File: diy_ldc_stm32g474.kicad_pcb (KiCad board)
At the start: 2 copper layers, 50.2 x 40 mm, 91 parts, among them J1 USB_B_Micro, J10 Conn_02x03_Odd_Even, J12 Conn_01x04, J13 Conn_01x05, J2 Conn_01x02, J3 Conn_01x03, J4 Conn_01x04, J6 Conn_Coaxial, J7 Conn_Coaxial, J8 Conn_Coaxial, J9 Conn_Coaxial, U1 XC6206PxxxMR, U2 STM32G431CBUx, U3 SN74LVC2G14DBV, U4 SN74LVC2G14DBV, U5 TPH2502-SR, U6 TLV2333IDR, U7 TPS61040DBV, U8 OPA2188AIDR, Y1 24MHz, 9pF

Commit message: WIP
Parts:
- moved C23 0.80 mm to (171.9, 71.5)
- moved R11 0.80 mm to (176.0, 73.9)
- moved R12 0.80 mm to (172.7, 73.9)
- moved R13 0.80 mm to (174.4, 73.9)
- moved R14 0.80 mm to (171.1, 73.9)
- moved H1 0.07 mm to (143.2, 63.4)
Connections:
- L1 pad 2: +3.3V -> +3V3
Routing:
- net GND: track 0.00 -> 10.1 mm, vias 0 -> 15
- net Net-(U2-PF0): track 0.00 -> 6.36 mm
- net +5V_IN: track 0.00 -> 5.69 mm
- net +3V3: track 0.00 -> 5.38 mm, vias 0 -> 4
- net Net-(C13-Pad1): track 0.00 -> 4.92 mm
- net /MCU/VREF+: track 0.00 -> 4.02 mm
- net Net-(U8B--): track 0.00 -> 3.69 mm
- net Net-(U8A--): track 0.00 -> 3.68 mm
- net +18V: track 0.00 -> 2.83 mm
- net +5V: track 0.00 -> 2.74 mm
- net Net-(U2-PF1): track 0.00 -> 2.24 mm
- net /MCU/piezo_drive/DAC1_CH1_GAIN: track 0.00 -> 2.22 mm
- net /MCU/NRST: track 0.00 -> 1.30 mm
- net /MCU/BOOT0: track 0.00 -> 1.26 mm
- added copper zone on F.Cu, net +3V3
- added copper zone on In2.Cu, net +3V3
- added copper zone on F.Cu, net +5V
- added copper zone on F.Cu, net +5V_IN
- added copper zone on F.Cu, net GND
- added copper zone on In1.Cu, net GND
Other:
- copper layers 2 -> 4
- board text added: "CLK"
- board text added: "DIO"
- board text added: "INV OUT0"
- board text added: "INV OUT1"
- board text removed: "INV_OUT0"
- board text removed: "INV_OUT1"

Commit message: Routing
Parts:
- moved J12 7.78 mm to (188.4, 78.8), turned to 180 degrees
- moved C31 3.88 mm to (153.3, 90.3), turned to -90 degrees
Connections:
- net Net-(U2-PA11) renamed /MCU/USB_MCU_D-
- net Net-(U2-PA12) renamed /MCU/USB_MCU_D+
- J1 pad 2: /MCU/Power/USB_D- -> /MCU/USB_D-
- J1 pad 3: /MCU/Power/USB_D+ -> /MCU/USB_D+
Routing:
- net +5V: track 2.74 -> 41.1 mm, vias 0 -> 4
- net +18V: track 2.83 -> 18.6 mm
- net /MCU/piezo_record_needle/PIEZO_IN_B: track 0.00 -> 15.0 mm
- net /MCU/piezo_drive/DAC1_CH1_GAIN: track 2.22 -> 17.1 mm
- net /MCU/USB_D-: track 0.00 -> 11.6 mm
- net /MCU/USB_D+: track 0.00 -> 11.1 mm
- net /MCU/piezo_record_needle/Vhalf: track 0.00 -> 10.8 mm
- net /MCU/piezo_drive/DAC1_CH2_GAIN: track 0.00 -> 8.81 mm
- net Net-(U5A--): track 0.00 -> 7.73 mm
- net +3V3: track 5.38 -> 11.6 mm, vias 4 -> 8
- net /MCU/piezo_record_needle/PIEZO_IN_A: track 0.00 -> 6.03 mm
- net GND: track 10.1 -> 4.32 mm, vias 15 -> 2
- net Net-(U6B--): track 0.00 -> 5.60 mm
- net Net-(U6A--): track 0.00 -> 5.43 mm
- net Net-(U7-FB): track 0.00 -> 5.07 mm
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- added copper zone on F.Cu, net +18V
- added copper zone on F.Cu, net Net-(D3-A)

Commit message: Preliminary routing done
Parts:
- moved J9 12.9 mm to (161.3, 64.0)
- moved J8 12.8 mm to (174.0, 64.0)
- moved C22 7.66 mm to (164.5, 77.2)
- moved R17 4.07 mm to (158.8, 73.5), turned to 90 degrees
- moved R18 1.85 mm to (162.0, 73.5)
- moved R16 1.47 mm to (160.4, 73.5)
- moved R15 1.31 mm to (157.3, 73.5)
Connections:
- J10 pad 1: /MCU/SPI3_SCK -> /MCU/SPI3_MISO
- J10 pad 3: /MCU/SPI3_MOSI -> /MCU/SPI3_SCK
- J10 pad 5: /MCU/SPI3_MISO -> /MCU/SPI3_MOSI
- J13 pad 1: /MCU/piezo_drive/dac1_out1 -> /MCU/dac1_out2
- J13 pad 2: /MCU/piezo_drive/dac1_out2 -> /MCU/dac1_out1
- J4 pad 2: /MCU/opamp2_vinp -> /MCU/opamp3_vinp
- J4 pad 3: /MCU/opamp3_vinp -> /MCU/opamp2_vinp
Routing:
- net /MCU/TIM4_ETR: track 0.00 -> 38.7 mm, vias 0 -> 2
- net GND: track 4.32 -> 42.5 mm, vias 2 -> 43
- net /MCU/opamp1_vinp: track 3.77 -> 40.1 mm, vias 0 -> 3
- net /MCU/TIM3_ETR: track 0.00 -> 34.5 mm
- net /MCU/SPI3_MISO: track 0.00 -> 34.4 mm, vias 0 -> 1
- net /MCU/SPI3_SCK: track 0.00 -> 33.1 mm, vias 0 -> 1
- net /MCU/opamp2_vinp: track 3.85 -> 36.7 mm, vias 0 -> 2
- net /MCU/BOOST_EN: track 0.00 -> 31.2 mm
- net /MCU/SPI3_MOSI: track 0.00 -> 29.4 mm, vias 0 -> 1
- net /MCU/TIM1_ETR: track 4.31 -> 32.4 mm, vias 0 -> 4
- net /MCU/dac1_out2: track 0.00 -> 20.9 mm, vias 0 -> 2
- net /MCU/dac1_out1: track 0.00 -> 20.2 mm, vias 0 -> 2
- net /MCU/TIM2_ETR: track 0.00 -> 17.2 mm
- net Net-(J7-In): track 0.00 -> 13.9 mm
- net /MCU/opamp3_vinp: track 0.00 -> 13.7 mm
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
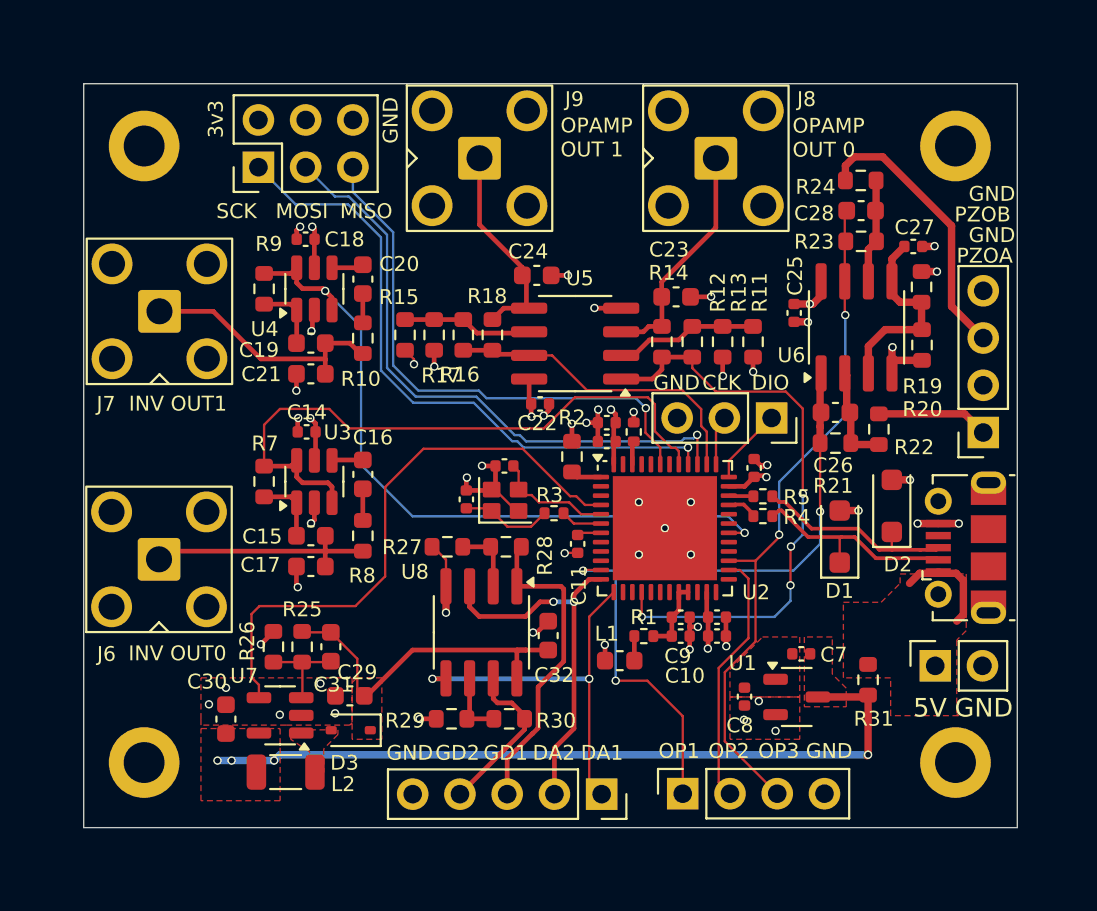
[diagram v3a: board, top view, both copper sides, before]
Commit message: changed 1 instance of Inverter oscillator
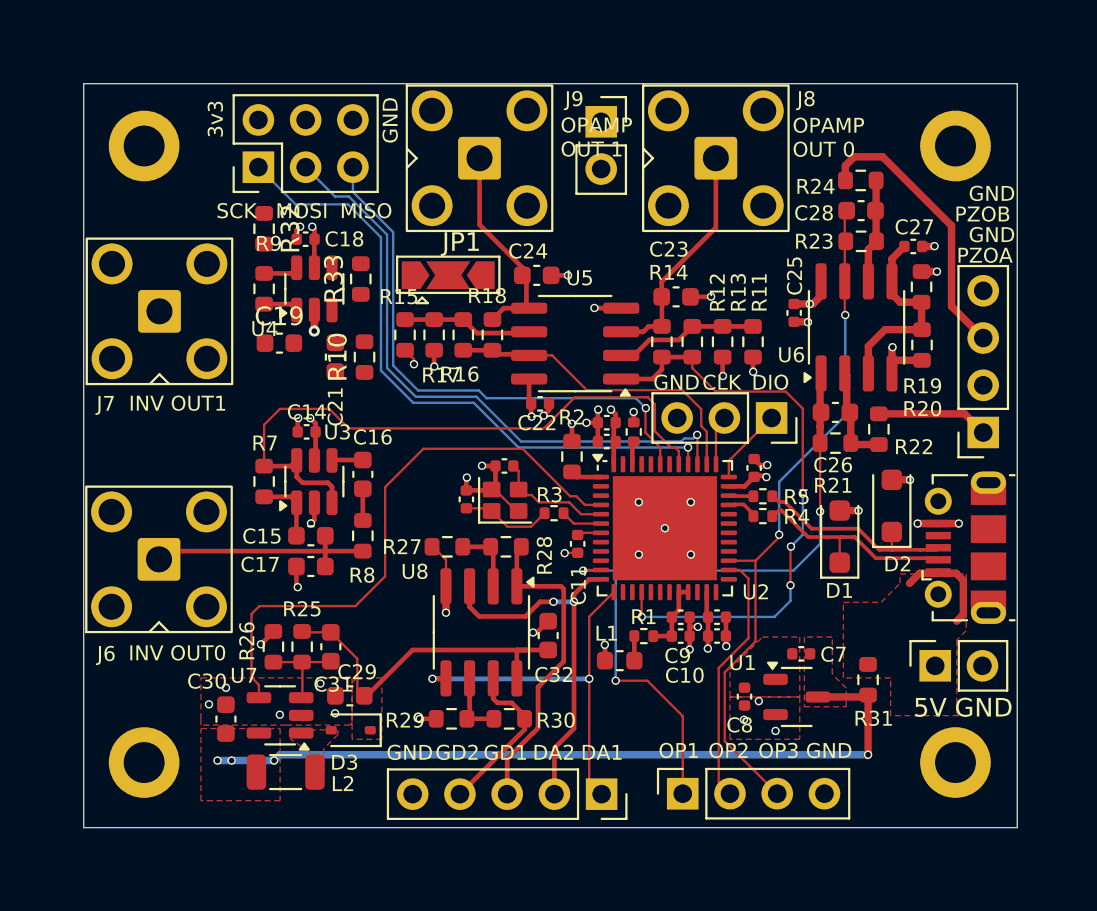
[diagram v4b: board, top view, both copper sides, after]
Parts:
- removed C20: 10n, Capacitor_SMD:C_0603_1608Metric
- added J5: Conn_01x02, Connector_PinSocket_2.54mm:PinSocket_1x02_P2.54mm_Vertical, F.Cu at (167.8, 62.0)
- added JP1: SolderJumper_3_Open, Jumper:SolderJumper-3_P2.0mm_Open_TrianglePad1.0x1.5mm, F.Cu at (159.6, 70.3)
- added R32: 49.9, Resistor_SMD:R_0603_1608Metric, F.Cu at (149.7, 67.8)
- added R33: 49.9, Resistor_SMD:R_0603_1608Metric, F.Cu at (154.9, 70.5)
- C19: value 10n -> 1n
- R10: value 10k -> 10Meg
- moved C19 1.69 mm to (150.5, 74.0), turned to 0 degrees
- moved C21 1.60 mm to (153.5, 74.7), turned to 90 degrees
- moved R10 1.02 mm to (155.1, 74.7), turned to 90 degrees
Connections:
- C21 pad 1: GND -> Net-(J5-Pin_2)
- C21 pad 2: Net-(J7-In) -> Net-(U4-2A)
- J7 pad 2: GND -> Net-(J7-Ext)
- R10 pad 1: Net-(C20-Pad2) -> GND
- R10 pad 2: Net-(J7-In) -> Net-(U4-2A)
- R9 pad 1: Net-(U4-1A) -> GND
- R9 pad 2: /MCU/TIM4_ETR -> Net-(U4-1A)
- U4 pad 3: /MCU/TIM4_ETR -> Net-(U4-2A)
- U4 pad 4: Net-(U4-2Y) -> /MCU/logic_gate_ldc/out2
- U4 pad 6: /MCU/TIM4_ETR -> /MCU/logic_gate_ldc/out1
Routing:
- net /MCU/TIM4_ETR: track 38.7 -> 1.88 mm, vias 2 -> 0
- net Net-(J7-In): track 13.9 -> 0.00 mm
- net Net-(U4-1A): track 3.67 -> 1.88 mm
- net Net-(U4-2Y): track 1.72 -> 0.00 mm
- net Net-(C20-Pad2): track 1.58 -> 0.00 mm
- net GND: track 42.5 -> 41.6 mm, vias 43 -> 42

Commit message: routing
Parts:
- moved C19 5.61 mm to (149.7, 68.4), turned to 90 degrees
- moved R32 1.62 mm to (151.2, 68.4)
- moved C18 1.45 mm to (152.9, 69.4), turned to 0 degrees
- moved R33 1.43 mm to (154.9, 71.9)
- moved R9 1.03 mm to (149.7, 72.1)
- moved U4 1.03 mm to (152.4, 72.1)
- moved C21 1.03 mm to (153.5, 75.7)
- moved R10 1.03 mm to (155.1, 75.7)
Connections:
- C19 pad 1: Net-(J7-In) -> Net-(J7-Ext)
- C19 pad 2: Net-(U4-1A) -> Net-(C19-Pad2)
- R32 pad 1: Net-(J7-Ext) -> Net-(C19-Pad2)
- R9 pad 2: Net-(U4-1A) -> Net-(J7-In)
- U4 pad 1: Net-(U4-1A) -> Net-(J7-In)
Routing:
- net Net-(J7-Ext): track 0.00 -> 18.6 mm
- net Net-(J7-In): track 0.00 -> 9.05 mm
- net Net-(U4-1A): track 1.88 -> 0.00 mm
- net /MCU/TIM4_ETR: track 1.88 -> 0.00 mm
- net /MCU/logic_gate_ldc/out1: track 0.00 -> 1.80 mm
- net /MCU/logic_gate_ldc/out2: track 0.00 -> 1.62 mm
- net Net-(C19-Pad2): track 0.00 -> 1.52 mm

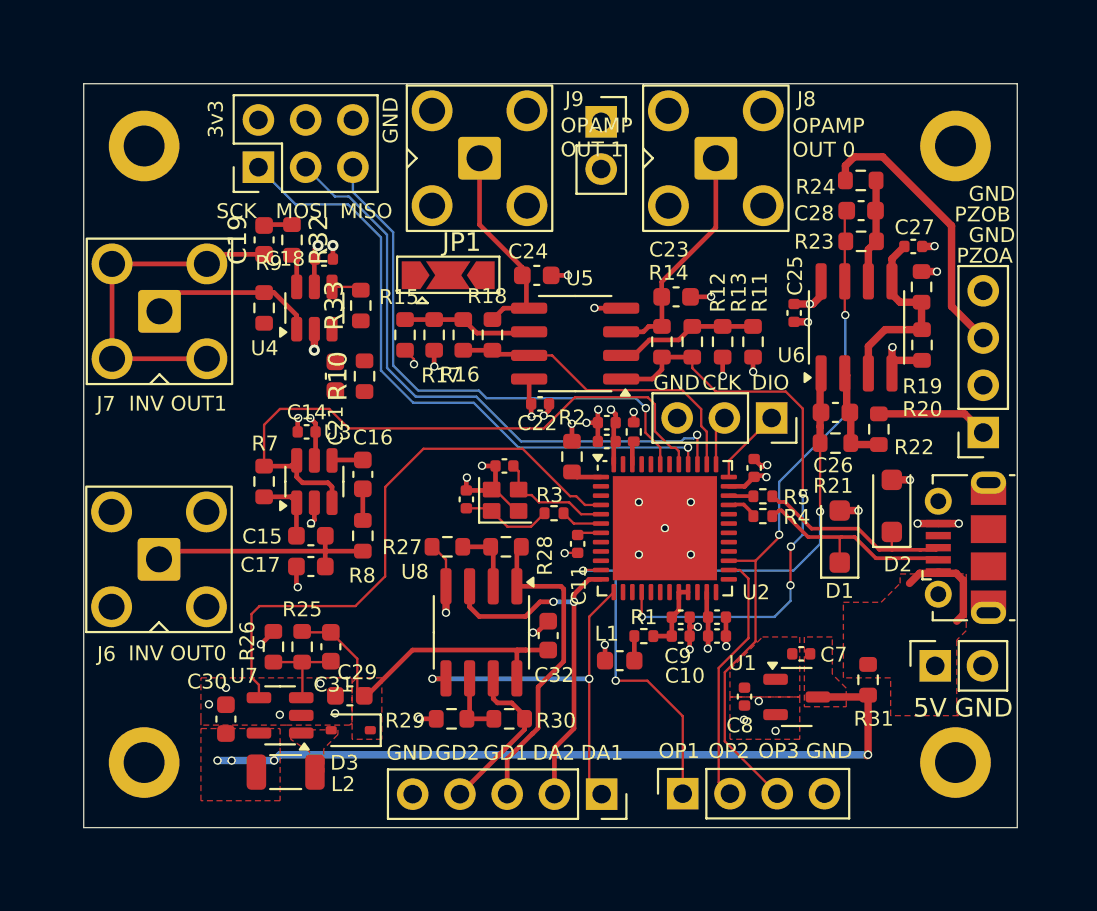
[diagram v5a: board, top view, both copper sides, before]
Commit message: Finisher re-routing with new inverter oscillators
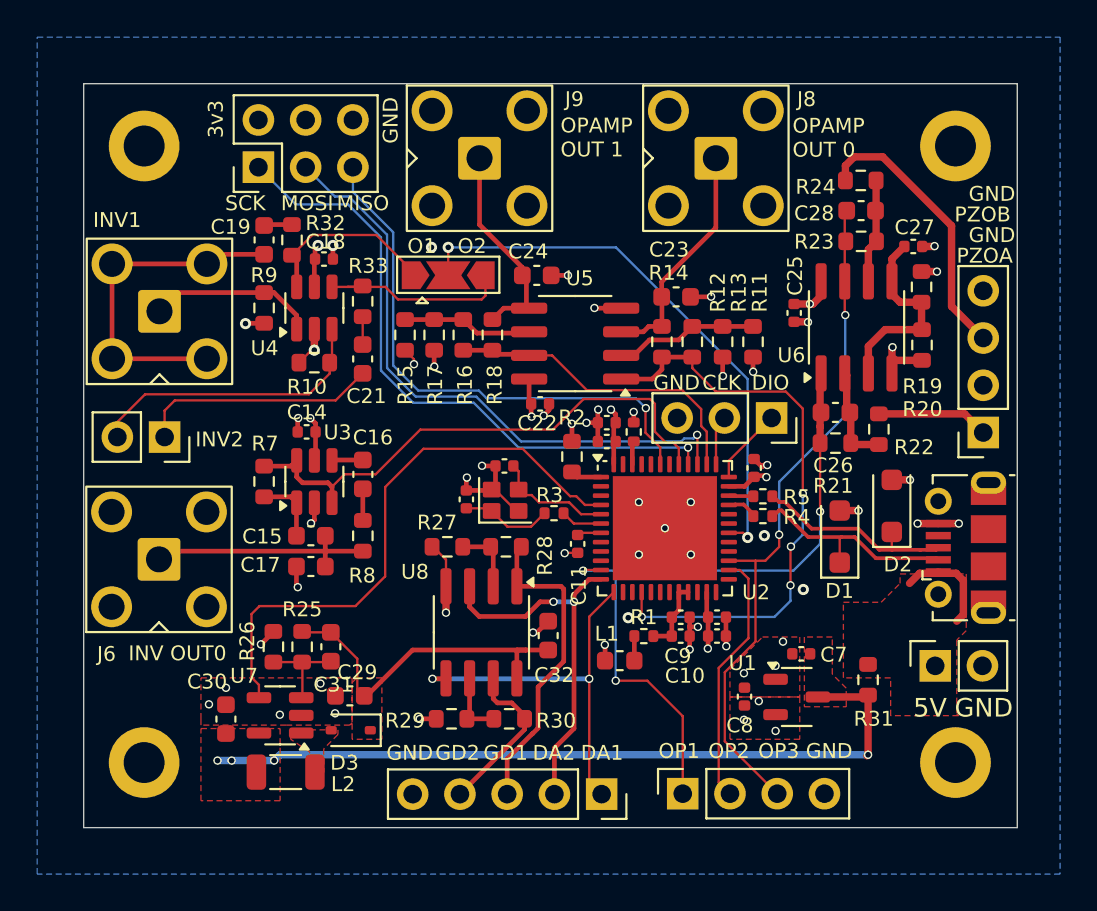
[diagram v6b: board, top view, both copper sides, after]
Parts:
- moved J5 29.0 mm to (144.3, 79.0), turned to -90 degrees
- moved R10 2.80 mm to (152.4, 75.0), turned to 0 degrees
- moved C21 1.74 mm to (155.0, 74.8), turned to -90 degrees
- moved R33 0.25 mm to (155.0, 71.7)
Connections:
- C21 pad 1: Net-(J5-Pin_2) -> Net-(C21-Pad1)
- C21 pad 2: Net-(U4-2A) -> Net-(J5-Pin_1)
- JP1 pad 2: /MCU/TIM3_ETR -> /MCU/TIM4_ETR
- R10 pad 2: Net-(U4-2A) -> Net-(J5-Pin_2)
- R33 pad 1: Net-(J5-Pin_1) -> Net-(C21-Pad1)
- U4 pad 3: Net-(U4-2A) -> Net-(J5-Pin_2)
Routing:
- net /MCU/TIM4_ETR: track 0.00 -> 30.2 mm, vias 0 -> 2
- net Net-(J5-Pin_2): track 0.00 -> 15.7 mm
- net Net-(J5-Pin_1): track 0.00 -> 12.9 mm
- net /MCU/logic_gate_ldc/out2: track 1.62 -> 10.4 mm
- net /MCU/logic_gate_ldc/out1: track 1.80 -> 9.73 mm
- net /MCU/TIM3_ETR: track 34.5 -> 29.2 mm
- net GND: track 41.5 -> 43.7 mm, vias 42 -> 50
- net Net-(C21-Pad1): track 0.00 -> 1.50 mm
- added copper zone on B.Cu, net GND
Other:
- board text added: "INV1"
- board text added: "INV2"
- board text added: "O1"
- board text added: "O2"
- board text removed: "INV OUT1"

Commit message: Done for now
Will breadboard oscillators before sending order out
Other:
- board text added: "INV0"
- board text removed: "INV OUT0"
- board text removed: "O1"
- board text removed: "O2"
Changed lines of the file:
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@@
 			(at -5.0935 -2.825 180)
 			(layer "F.SilkS")
+			(hide yes)
 			(effects
 				(font
@@
 		)
 	)
-	(gr_text "O1"
-		(at 157.4 69.2 0)
+	(gr_text "INV1"
+		(at 156.8 69.2 0)
 		(layer "F.SilkS")
 		(effects
@@
 		)
 	)
-	(gr_text "O2"
-		(at 160.1 69.2 0)
+	(gr_text "INV2"
+		(at 159.7 69.2 0)
 		(layer "F.SilkS")
 		(effects
@@
 		)
 	)
-	(gr_text "INV OUT0"
-		(at 142.4 91.1 0)
+	(gr_text "INV0"
+		(at 140.5 91.1 0)
 		(layer "F.SilkS")
 		(effects
